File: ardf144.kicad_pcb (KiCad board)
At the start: 2 copper layers, 150 x 30.2 mm, 59 parts, among them J1 Jack-DC, J2 batt, J3 ant, Q1 2SC1906, SW1 SW_SPST, U1 NE612, U2 2SK439, U3 L7805, U4 LM386, U5 2SK439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

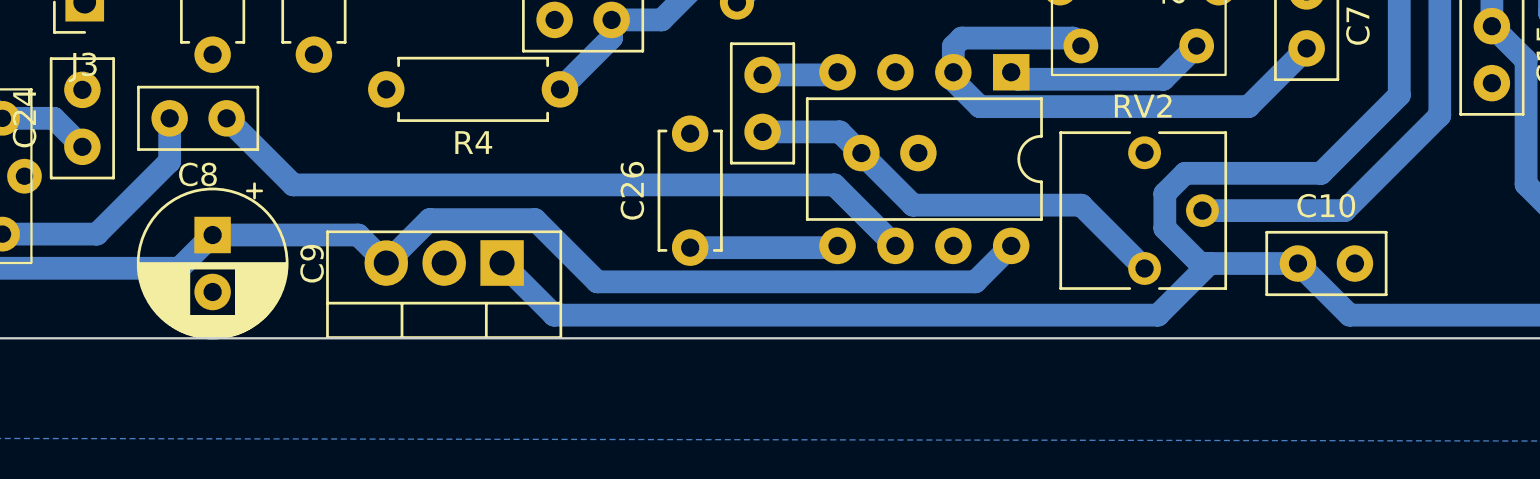
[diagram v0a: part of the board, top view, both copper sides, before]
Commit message: fix attiny vcc +3v3 from +5v
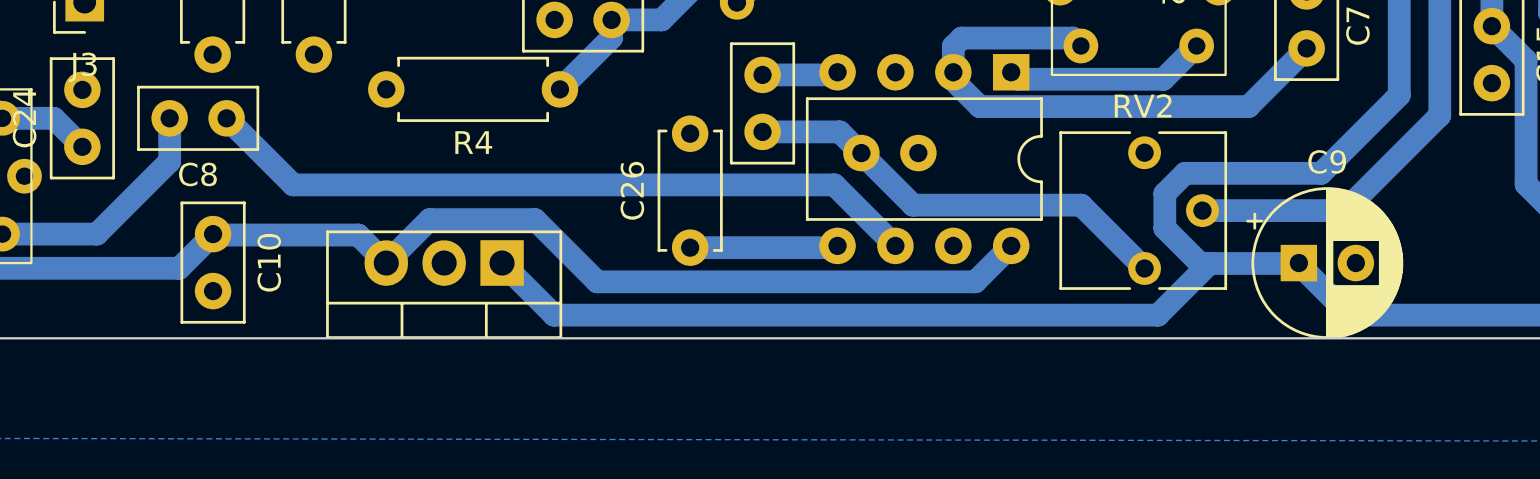
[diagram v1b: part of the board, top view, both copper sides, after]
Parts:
- C19: value 100u -> 100p
- C2: value 3u -> 3p
- C20: value 150u -> 100p
- C21: value 15u -> 15p
- C23: value 5u -> 5p
- C4: value 5 -> 5p
- moved C9 47.7 mm to (132.8, 61.0), turned to 0 degrees
- moved C10 47.6 mm to (85.1, 59.7), turned to -90 degrees
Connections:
- C10 pad 1: 9v -> 5v
- C9 pad 1: 5v -> 9v
- L1 pad : GND -> (no net)
- L2 pad : GND -> (no net)
- L4 pad : GND -> (no net)
- L5 pad : GND -> (no net)
